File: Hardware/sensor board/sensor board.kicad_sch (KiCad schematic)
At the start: 5 parts, among them J1 Raspberry_Pi_2_3

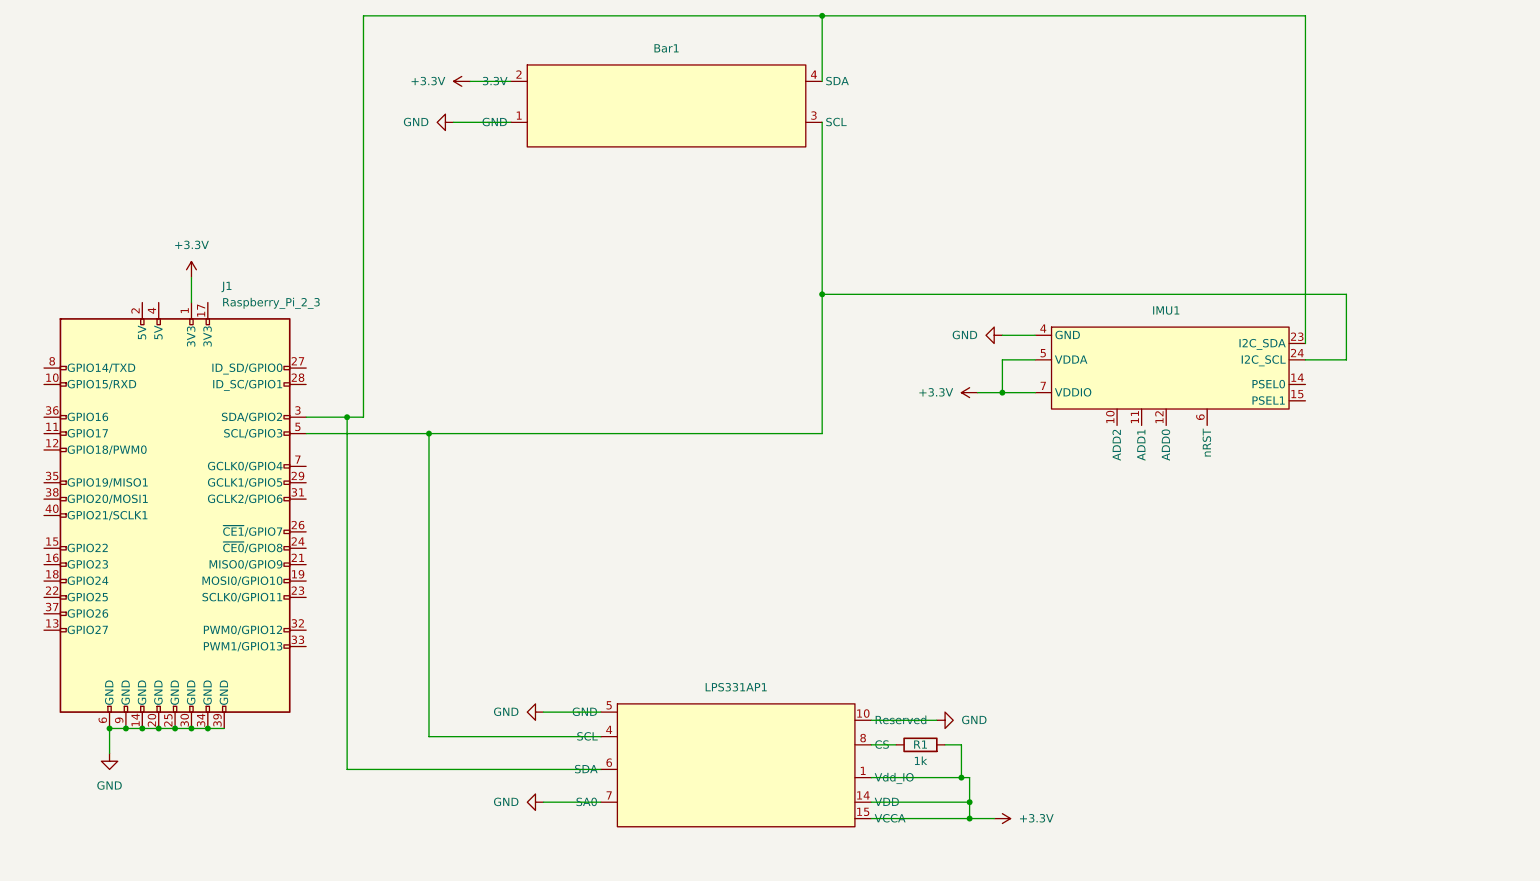
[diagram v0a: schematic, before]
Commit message: Added separate sheet for IMU and added connector footprint to Bar30 and resistor
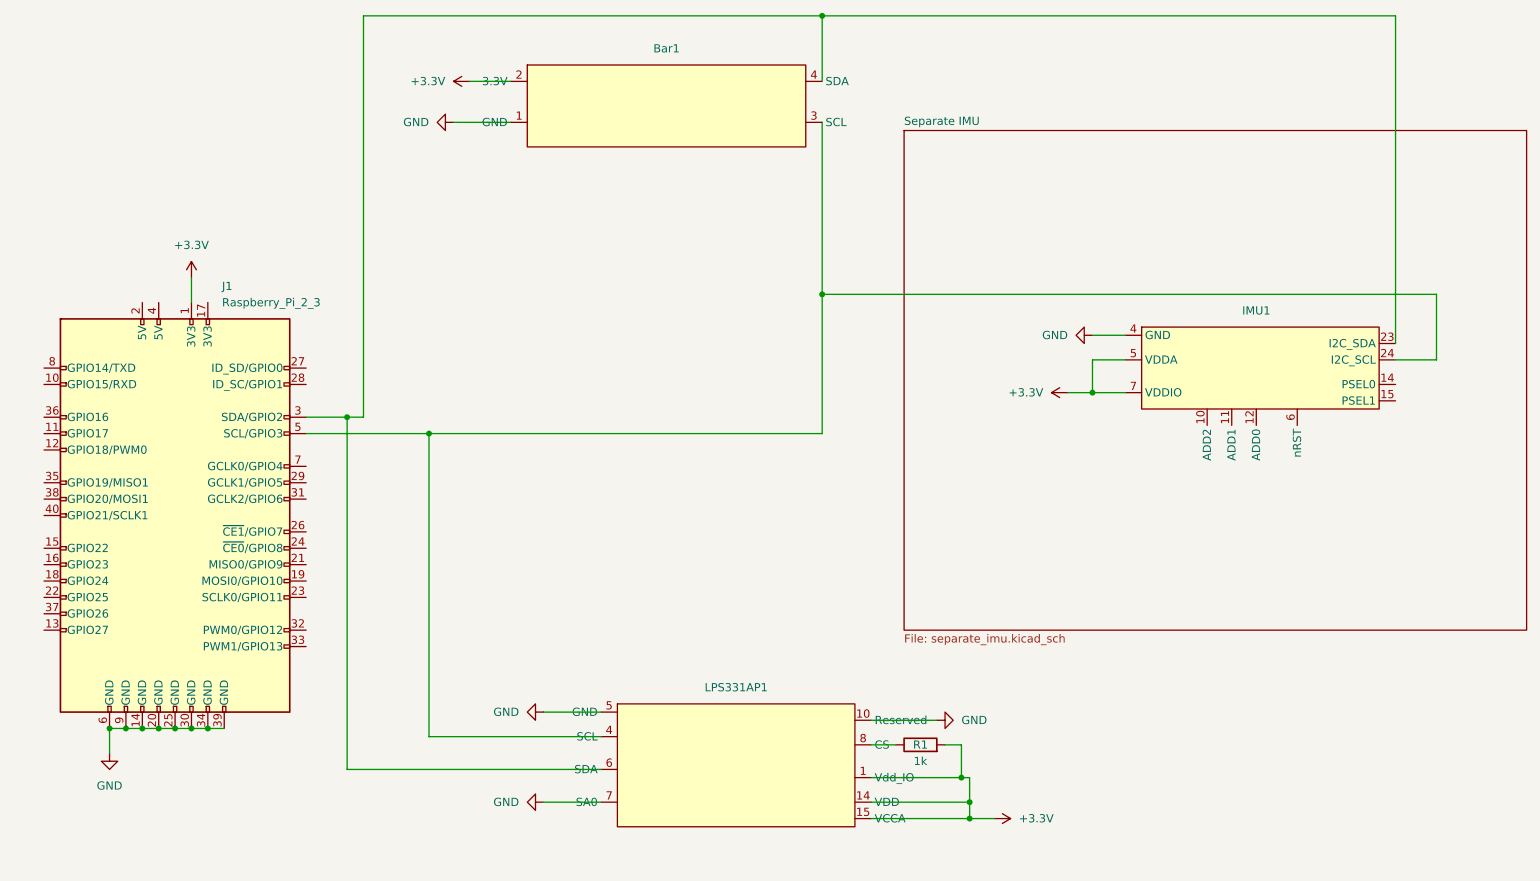
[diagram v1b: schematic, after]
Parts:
- Bar1: footprint (none) -> Connector_JST:JST_GH_BM04B-GHS-TBT_1x04-1MP_P1.25mm_Vertical
- R1: footprint (none) -> Resistor_SMD:R_0805_2012Metric
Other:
- added sheet Separate IMU (separate_imu.kicad_sch)
- moved on the sheet: IMU1
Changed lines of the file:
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@@
   (junction (at 162.56 69.85) (diameter 0) (color 0 0 0 0)
   )
-  (junction (at 190.5 85.09) (diameter 0) (color 0 0 0 0)
+  (junction (at 204.47 85.09) (diameter 0) (color 0 0 0 0)
   )
   (junction (at 101.6 91.44) (diameter 0) (color 0 0 0 0)
@@
     (stroke (width 0) (type default))
   )
-  (wire (pts (xy 237.49 77.47) (xy 237.49 26.67))
+  (wire (pts (xy 251.46 77.47) (xy 251.46 26.67))
     (stroke (width 0) (type default))
   )
@@
     (stroke (width 0) (type default))
   )
-  (wire (pts (xy 243.84 69.85) (xy 162.56 69.85))
+  (wire (pts (xy 257.81 69.85) (xy 162.56 69.85))
     (stroke (width 0) (type default))
   )
@@
     (stroke (width 0) (type default))
   )
-  (wire (pts (xy 190.5 80.01) (xy 190.5 85.09))
+  (wire (pts (xy 204.47 80.01) (xy 204.47 85.09))
     (stroke (width 0) (type default))
   )
@@
     (stroke (width 0) (type default))
   )
-  (wire (pts (xy 186.69 85.09) (xy 190.5 85.09))
+  (wire (pts (xy 200.66 85.09) (xy 204.47 85.09))
     (stroke (width 0) (type default))
   )
@@
     (stroke (width 0) (type default))
   )
-  (wire (pts (xy 237.49 26.67) (xy 162.56 26.67))
-    (stroke (width 0) (type default))
-  )
-  (wire (pts (xy 237.49 80.01) (xy 243.84 80.01))
-    (stroke (width 0) (type default))
-  )
-  (wire (pts (xy 190.5 85.09) (xy 195.58 85.09))
+  (wire (pts (xy 251.46 26.67) (xy 162.56 26.67))
+    (stroke (width 0) (type default))
+  )
+  (wire (pts (xy 251.46 80.01) (xy 257.81 80.01))
+    (stroke (width 0) (type default))
+  )
+  (wire (pts (xy 204.47 85.09) (xy 209.55 85.09))
     (stroke (width 0) (type default))
   )
@@
     (stroke (width 0) (type default))
   )
-  (wire (pts (xy 243.84 80.01) (xy 243.84 69.85))
+  (wire (pts (xy 257.81 80.01) (xy 257.81 69.85))
     (stroke (width 0) (type default))
   )
@@
     (stroke (width 0) (type default))
   )
-  (wire (pts (xy 195.58 80.01) (xy 190.5 80.01))
+  (wire (pts (xy 209.55 80.01) (xy 204.47 80.01))
     (stroke (width 0) (type default))
   )
@@
     (stroke (width 0) (type default))
   )
-  (wire (pts (xy 190.5 76.2) (xy 195.58 76.2))
+  (wire (pts (xy 204.47 76.2) (xy 209.55 76.2))
     (stroke (width 0) (type default))
   )
@@
     )
   )
-  (symbol (lib_id "power:GND") (at 190.5 76.2 270) (unit 1)
-    (in_bom yes) (on_board yes) (dnp no) (fields_autoplaced)
-    (property "Reference" "#PWR010" (at 184.15 76.2 0)
-      (effects (font (size 1.27 1.27)) hide)
-    )
-    (property "Value" "GND" (at 186.69 76.2 90)
+  (symbol (lib_id "power:GND") (at 204.47 76.2 270) (unit 1)
+    (in_bom yes) (on_board yes) (dnp no) (fields_autoplaced)
+    (property "Reference" "#PWR010" (at 198.12 76.2 0)
+      (effects (font (size 1.27 1.27)) hide)
+    )
+    (property "Value" "GND" (at 200.66 76.2 90)
       (effects (font (size 1.27 1.27)) (justify right))
     )
-    (property "Footprint" "" (at 190.5 76.2 0)
-      (effects (font (size 1.27 1.27)) hide)
-    )
-    (property "Datasheet" "" (at 190.5 76.2 0)
+    (property "Footprint" "" (at 204.47 76.2 0)
+      (effects (font (size 1.27 1.27)) hide)
+    )
+    (property "Datasheet" "" (at 204.47 76.2 0)
       (effects (font (size 1.27 1.27)) hide)
     )
@@
       (effects (font (size 1.27 1.27)))
     )
-    (property "Footprint" "" (at 177.8 141.478 90)
+    (property "Footprint" "Resistor_SMD:R_0805_2012Metric" (at 177.8 141.478 90)
       (effects (font (size 1.27 1.27)) hide)
     )
@@
       (effects (font (size 1.27 1.27)))
     )
-    (property "Footprint" "" (at 138.43 31.75 0)
+    (property "Footprint" "Connector_JST:JST_GH_BM04B-GHS-TBT_1x04-1MP_P1.25mm_Vertical" (at 138.43 31.75 0)
       (effects (font (size 1.27 1.27)) hide)
     )
@@
     )
   )
-  (symbol (lib_name "MTi_1_1") (lib_id "New_Library:MTi_1") (at 215.9 73.66 0) (unit 1)
+  (symbol (lib_name "MTi_1_1") (lib_id "New_Library:MTi_1") (at 229.87 73.66 0) (unit 1)
     (in_bom yes) (on_board yes) (dnp no)
-    (property "Reference" "IMU1" (at 215.9 72.39 0)
-      (effects (font (size 1.27 1.27)))
-    )
-    (property "Value" "~" (at 215.9 73.66 0)
-      (effects (font (size 1.27 1.27)))
-    )
-    (property "Footprint" "" (at 215.9 73.66 0)
-      (effects (font (size 1.27 1.27)) hide)
-    )
-    (property "Datasheet" "" (at 215.9 73.66 0)
+    (property "Reference" "IMU1" (at 229.87 72.39 0)
+      (effects (font (size 1.27 1.27)))
+    )
+    (property "Value" "~" (at 229.87 73.66 0)
+      (effects (font (size 1.27 1.27)))
+    )
+    (property "Footprint" "" (at 229.87 73.66 0)
+      (effects (font (size 1.27 1.27)) hide)
+    )
+    (property "Datasheet" "" (at 229.87 73.66 0)
       (effects (font (size 1.27 1.27)) hide)
     )
@@
     )
   )
-  (symbol (lib_id "power:+3.3V") (at 186.69 85.09 90) (unit 1)
-    (in_bom yes) (on_board yes) (dnp no) (fields_autoplaced)
-    (property "Reference" "#PWR08" (at 190.5 85.09 0)
-      (effects (font (size 1.27 1.27)) hide)
-    )
-    (property "Value" "+3.3V" (at 182.88 85.09 90)
+  (symbol (lib_id "power:+3.3V") (at 200.66 85.09 90) (unit 1)
+    (in_bom yes) (on_board yes) (dnp no) (fields_autoplaced)
+    (property "Reference" "#PWR08" (at 204.47 85.09 0)
+      (effects (font (size 1.27 1.27)) hide)
+    )
+    (property "Value" "+3.3V" (at 196.85 85.09 90)
       (effects (font (size 1.27 1.27)) (justify left))
     )
-    (property "Footprint" "" (at 186.69 85.09 0)
-      (effects (font (size 1.27 1.27)) hide)
-    )
-    (property "Datasheet" "" (at 186.69 85.09 0)
+    (property "Footprint" "" (at 200.66 85.09 0)
+      (effects (font (size 1.27 1.27)) hide)
+    )
+    (property "Datasheet" "" (at 200.66 85.09 0)
       (effects (font (size 1.27 1.27)) hide)
     )
@@
       )
     )
+  )
+  (sheet (at 175.26 44.45) (size 96.52 77.47) (fields_autoplaced)
+    (stroke (width 0.1524) (type solid))
+    (fill (color 0 0 0 0.0000))
+    (property "Sheetname" "Separate IMU" (at 175.26 43.7384 0)
+      (effects (font (size 1.27 1.27)) (justify left bottom))
+    )
+    (property "Sheetfile" "separate_imu.kicad_sch" (at 175.26 122.5046 0)
+      (effects (font (size 1.27 1.27)) (justify left top))
+    )
+    (instances
+      (project "sensor board"
+        (path "/b809390c-5c7b-4faa-a505-ee668295313b" (page "2"))
+      )
+    )

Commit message: Modified sensor board and separate sheet for IMU
Added footprints to internal pressure sensor, made changes from 11/11
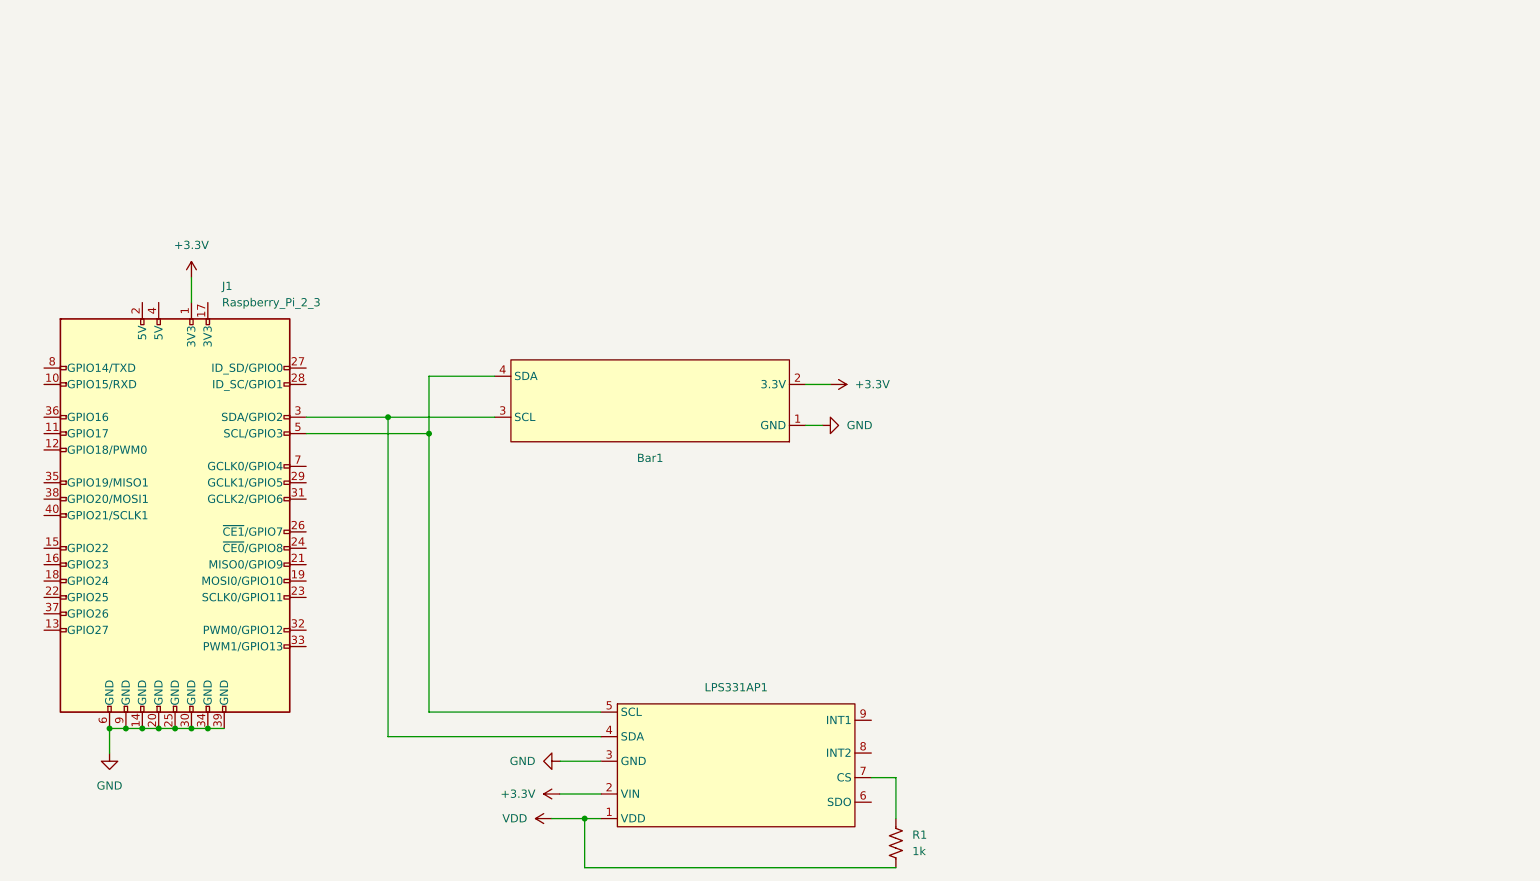
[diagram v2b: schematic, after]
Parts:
- removed IMU1: ~, symbol New_Library:MTi_1
- removed R1: 1k, Resistor_SMD:R_0805_2012Metric, symbol Device:R
- added R1: 1k, symbol Device:R_US
- LPS331AP1: footprint (none) -> Connector_PinHeader_2.54mm:PinHeader_1x09_P2.54mm_Vertical
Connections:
- net +3.3V: now also Bar1.2 (3.3V), LPS331AP1.2 (VIN)
- net GND: now also Bar1.1 (GND), LPS331AP1.3 (GND)
- net VDD: now reaches LPS331AP1.1 (VDD)
- net VDD: now also R1.2
- net at LPS331AP1.4 (SDA): now also Bar1.3 (SCL), J1.3 (SDA/GPIO2)
- net at LPS331AP1.5 (SCL): now also Bar1.4 (SDA), J1.5 (SCL/GPIO3)
- net at LPS331AP1.7 (CS): now also R1.1
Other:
- removed sheet Separate IMU
- moved on the sheet: Bar1, LPS331AP1

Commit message: added imu sheet block + second connector into main sheet, minor symbol edits
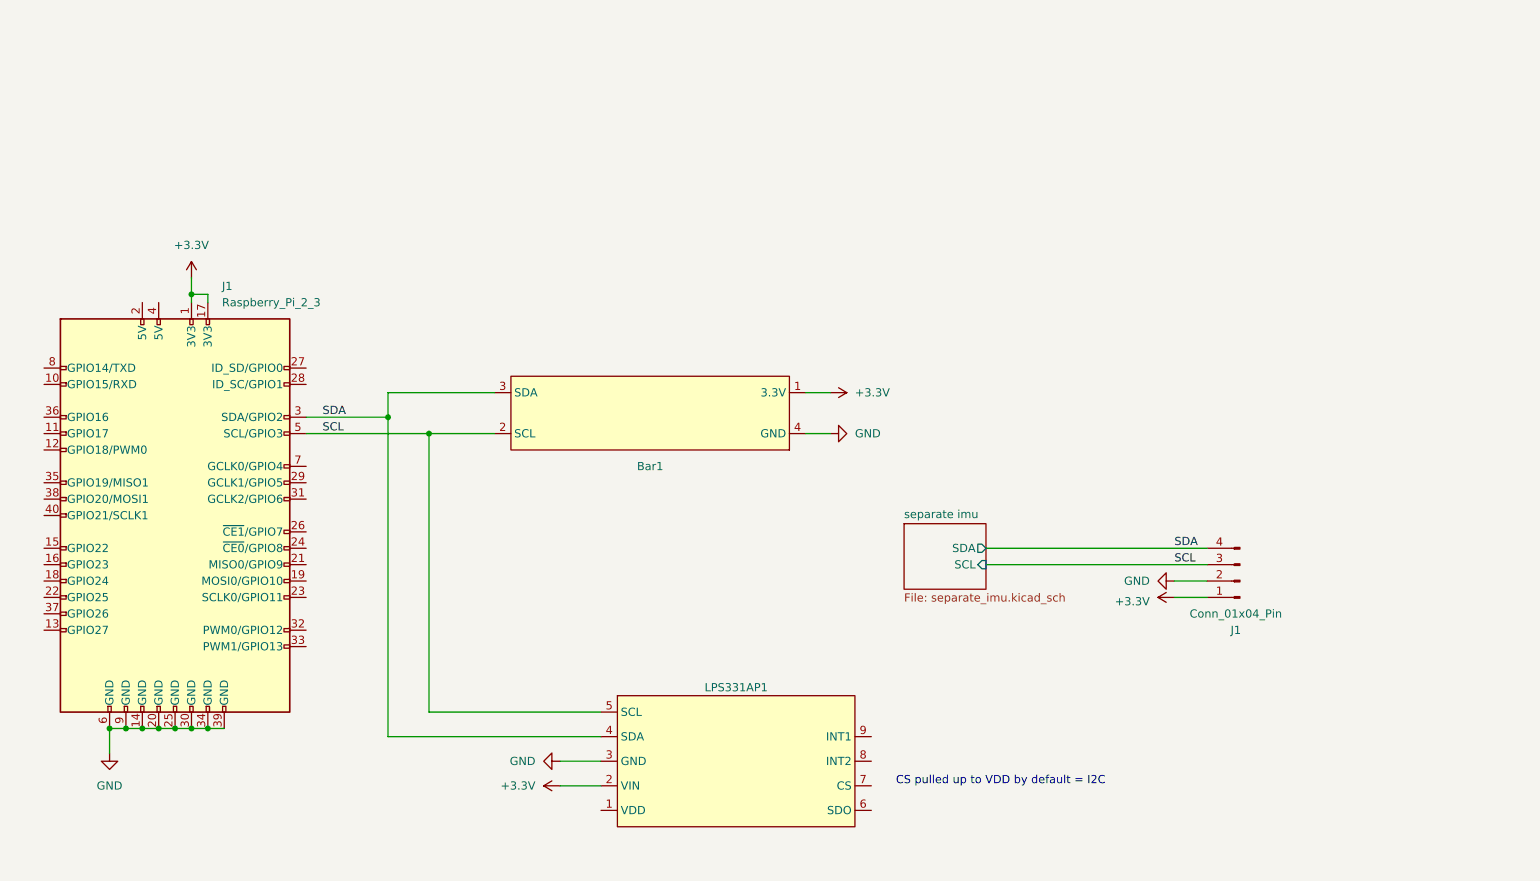
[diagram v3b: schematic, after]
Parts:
- removed R1: 1k, symbol Device:R_US
- added J1: Conn_01x04_Pin, symbol Connector:Conn_01x04_Pin
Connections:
- net +3.3V: now also Bar1.1 (3.3V), J1.17 (3V3), J1.1 (Pin_1); no longer Bar1.2 (3.3V)
- net GND: now also Bar1.4 (GND), J1.2 (Pin_2); no longer Bar1.1 (GND)
- net SDA: now reaches Bar1.3 (SDA), J1.3 (SDA/GPIO2), LPS331AP1.4 (SDA)
- net SDA: now also J1.4 (Pin_4)
- net SCL: now reaches J1.5 (SCL/GPIO3), LPS331AP1.5 (SCL)
- net SCL: now also Bar1.2 (SCL), J1.3 (Pin_3); no longer Bar1.4 (SDA)
- net VDD: no longer names the net of LPS331AP1.1 (VDD)
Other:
- added sheet separate imu (separate_imu.kicad_sch)
- note added: "CS pulled up to VDD by default = I2C"
- moved on the sheet: Bar1
